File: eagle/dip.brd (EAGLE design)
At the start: 63.2 x 20.3 mm, 9 parts

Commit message: inital V3 commit
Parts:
- removed JP6: M01PTH, SparkFun-Connectors:1X01
- added BAT1: (no value), SparkFun-Electromechanical:BATTCON_12MM
- added R1, R2, R3: RESISTOR, thewknd:R0805
- added S1: (no value), SparkFun-Electromechanical:TACTILE_SWITCH_SMD
- added SJ1, SJ2: (no value), SparkFun-Passives:SJ_2S-NO
- JP1, JP2: value M20 -> M14; device SparkFun-Connectors:1X20 -> SparkFun-Connectors:1X14
- JP5: device SparkFun-Connectors:1X03 -> SparkFun-Connectors:1X05
- JP8, JP9: value (none) -> M10"; device SparkFun-Connectors:1X04 -> SparkFun-Connectors:1X10
- moved JP1 15.9 mm to (34.9, 2.54)
- moved JP2 15.9 mm to (34.9, 17.8)
- moved JP5 5.71 mm to (4.45, 15.2)
- moved JP7 0.64 mm to (34.9, 5.08)
- moved JP3 0.64 mm to (17.1, 12.7)
- moved JP4 0.64 mm to (17.1, 10.2)
- moved JP8 0.63 mm to (60.3, 2.54)
- moved JP9 0.63 mm to (60.3, 17.8)
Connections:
- removed net 3V3: JP2.18
- new net +3V3: JP2.12, JP7.2, R3.2, SJ1.2, SJ2.2
- new net N$2: R2.2, SJ1.1
- new net N$3: R1.2, SJ2.1
- net A0: now also JP2.2; no longer JP2.8
- net A1: now also JP2.3; no longer JP2.9
- net A10: now also JP5.4; no longer JP5.2
- net A11: now also JP5.5; no longer JP5.3
- net A2: now also JP2.4; no longer JP2.10
- net A3: now also JP2.5; no longer JP2.11
- net A4: now also JP2.6, R2.1; no longer JP2.12
- net A5: now also JP2.7, R1.1; no longer JP2.13
- net A6: now also JP2.8; no longer JP2.14
- net A7: now also JP2.9; no longer JP2.15
- net A8: now also JP2.10; no longer JP2.16
- net A9: now also JP2.11; no longer JP2.17
- net AGND: now also JP2.13; no longer JP2.19
- net AREF: now also JP5.3, JP9.6; no longer JP2.2, JP5.1
- net D0: now also JP1.13; no longer JP1.19
- net D1: now also JP1.12; no longer JP1.18
- net D10: now also JP1.3; no longer JP1.9
- net D11: now also JP1.2; no longer JP1.8
- net D12: now also JP1.1; no longer JP1.7
- net D13: now also JP2.1; no longer JP2.7
- net D2: now also JP1.11; no longer JP1.17
- net D24: now also JP8.10; no longer JP1.6
- net D25: now also JP8.9; no longer JP1.5
- net D26: now also JP8.8; no longer JP1.4
- net D27: now also JP8.7; no longer JP1.3
- net D28: now also JP8.6; no longer JP1.2
- net D29: now also JP8.5; no longer JP1.1
- net D3: now also JP1.10; no longer JP1.16
- net D4: now also JP1.9; no longer JP1.15
- net D5: now also JP1.8; no longer JP1.14
- net D6: now also JP1.7; no longer JP1.13
- net D7: now also JP1.6; no longer JP1.12
- net D8: now also JP1.5; no longer JP1.11
- net D9: now also JP1.4; no longer JP1.10
- net GND: now also BAT1.GND, JP1.14, JP9.9, S1.3, S1.4; no longer JP1.20, JP2.5
- net PROG: now also JP9.5; no longer JP2.1
- net RESET: now also JP9.7, R3.1, S1.1, S1.2; no longer JP2.3
- net VBAT: now also BAT1.PWR@1, JP9.10; no longer JP2.6
- net VIN: now also JP2.14; no longer JP2.20
- net VUSB: now also JP5.1, JP9.8; no longer JP2.4, JP6.1
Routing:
- net +3V3: track 0.00 -> 35.8 mm, vias 0 -> 3
- net GND: track 7.77 -> 38.4 mm, vias 11 -> 16
- net A11: track 76.1 -> 48.9 mm, vias 1 -> 0
- net A10: track 79.4 -> 54.5 mm
- net VBAT: track 25.7 -> 47.6 mm, vias 0 -> 2
- net RESET: track 12.7 -> 26.1 mm, vias 1 -> 4
- net A4: track 0.00 -> 12.3 mm
- net A5: track 0.00 -> 11.9 mm
- net AREF: track 54.5 -> 44.8 mm, vias 1 -> 0
- net D30: track 29.3 -> 36.2 mm
- net N$5: track 0.00 -> 2.54 mm
- net N$3: track 0.00 -> 1.88 mm
- net N$2: track 0.00 -> 1.88 mm
- net D26: track 21.4 -> 23.2 mm, vias 0 -> 2
- net A13: track 39.2 -> 37.7 mm
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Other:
- board size 63.2 x 20.3 mm -> 67 x 20.3 mm
- board text added: "RESET"
- board text added: "REV. 003-0"
- board text added: "THANATOS"
- board text added: "Teensy 3.0 to breadboard adapter https://github.com/thewknd/Teensy3.0ToBreadboard This work is licensed under a Creative Commons Attribution-ShareAlike 3.0 Unported License. http://creativecommons.org/licenses/by-sa/3.0/ (c) 2012, 2013 Jonas Niggli (thewknd)"
- board text added: "git.io/M8cBRg"
- board text removed: "tinytiger.ch V000001"

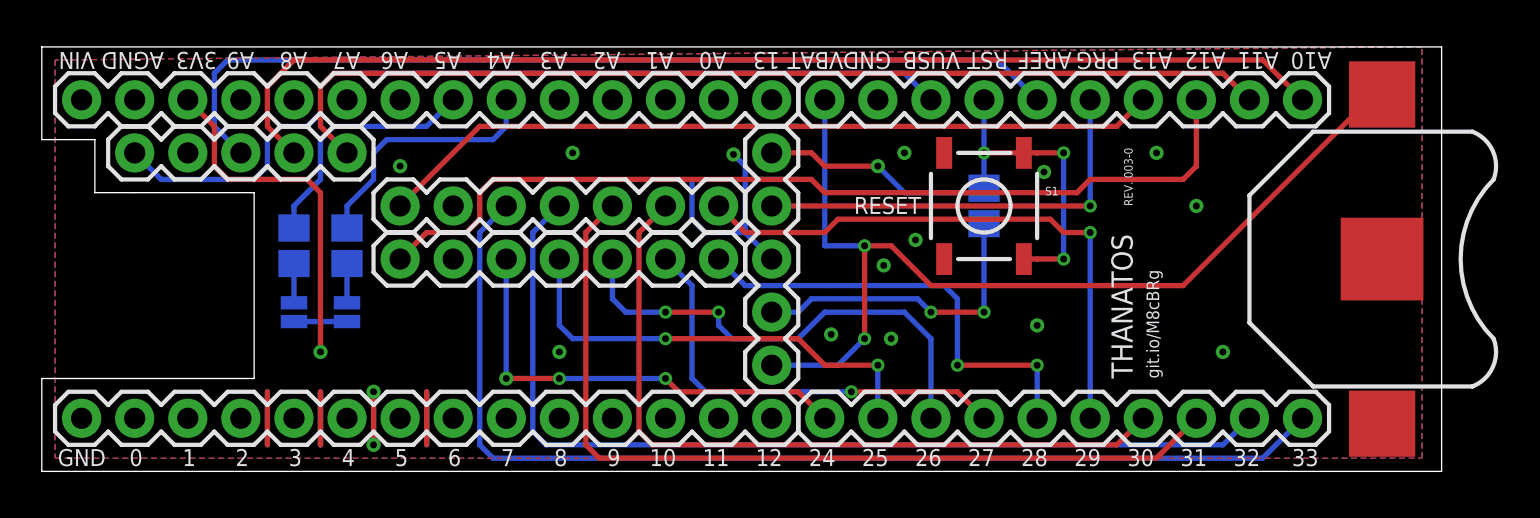
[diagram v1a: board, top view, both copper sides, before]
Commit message: new reset button
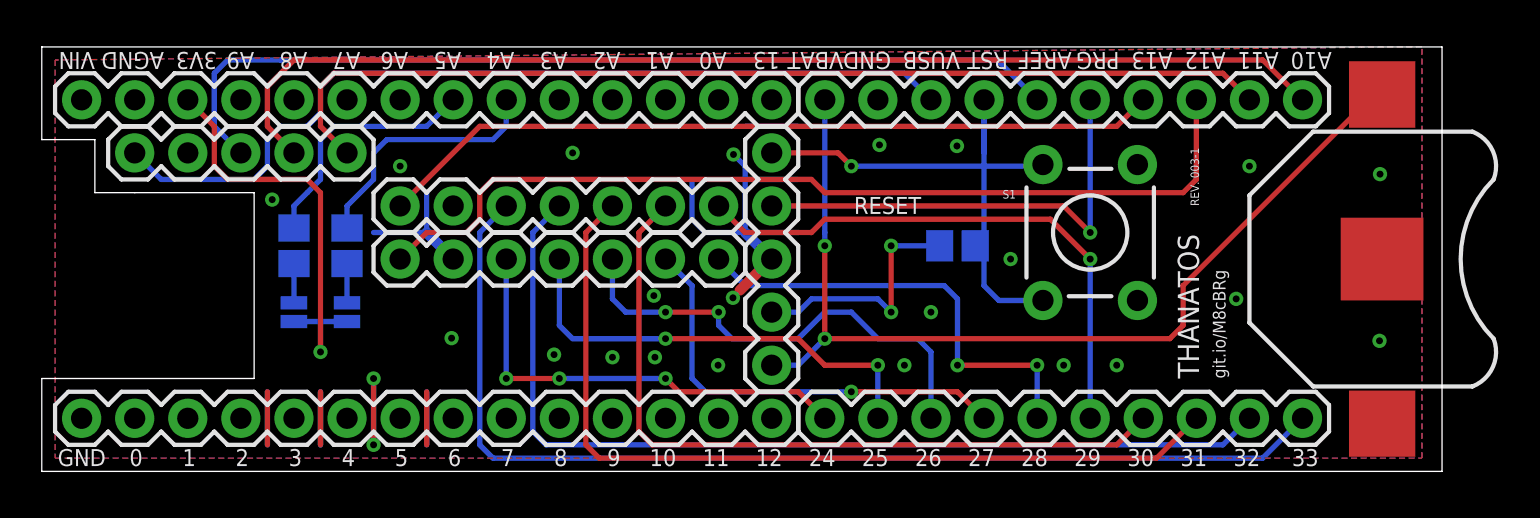
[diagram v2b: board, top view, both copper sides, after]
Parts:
- S1: value (none) -> SWITCH-PTH; device SparkFun-Electromechanical:TACTILE_SWITCH_SMD -> thewknd:SWITCH_PTH
- moved S1 5.24 mm to (50.2, 11.4), turned to 90 degrees
- moved R3 2.29 mm to (43.8, 10.8), turned to 0 degrees
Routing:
- net GND: track 38.4 -> 48.1 mm, vias 16 -> 24
- net +3V3: track 35.8 -> 32.7 mm
- net RESET: track 26.1 -> 28.2 mm, vias 4 -> 1
- net PROG: track 20.3 -> 22.1 mm
- net D29: track 27.7 -> 27.0 mm
- net VBAT: track 47.6 -> 47.1 mm
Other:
- board text added: "REV. 003-1"
- board text removed: "REV. 003-0"
- board text removed: "Teensy 3.0 to breadboard adapter This work is licensed under a Creative Commons Attribution-ShareAlike 3.0 Unported License. http://creativecommons.org/licenses/by-sa/3.0/ (c) 2012 Jonas Niggli (thewknd)"
